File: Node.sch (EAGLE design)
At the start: 63 parts, among them J1 DF12A3.0-14DS, Q1 16MHz, U1 ATMEGA32U4QFN, U2 NRF24L01NOPAD, U3 LTC3553, U4 L3GD20, U6 LSM303DLHC, U7 BD2425NNRF0404, U9 RCLAMP0502A, X1 USBSMD

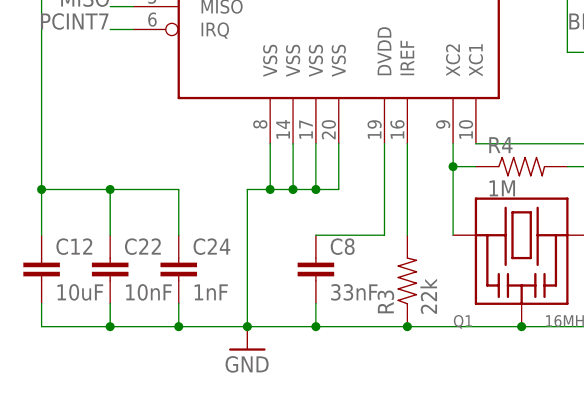
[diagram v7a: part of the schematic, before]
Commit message: start of base station
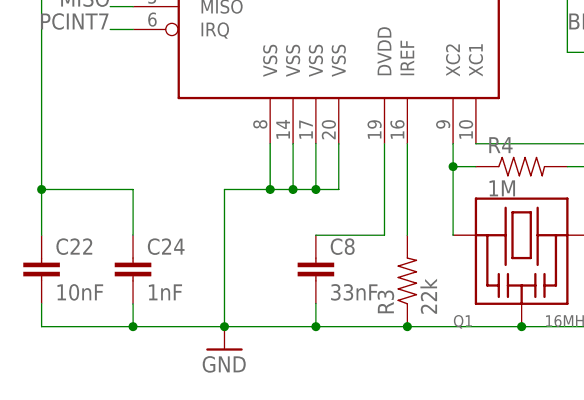
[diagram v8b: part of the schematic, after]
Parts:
- removed C12: 10uF, SparkFun:CAP0603-CAP
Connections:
- net +3V3: no longer C12.1
- net GND: no longer C12.2
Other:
- moved on the sheet: C22, C24
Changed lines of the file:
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@@
 <part name="GND9" library="supply1" deviceset="GND" device=""/>
 <part name="+3V8" library="supply1" deviceset="+3V3" device=""/>
-<part name="C12" library="SparkFun" deviceset="CAP" device="0603-CAP" value="10uF"/>
 <part name="C22" library="SparkFun" deviceset="CAP" device="0402-CAP" value="10nF"/>
 <part name="C24" library="SparkFun" deviceset="CAP" device="0402-CAP" value="1nF"/>
@@
 <instance part="U2" gate="G$1" x="43.18" y="48.26"/>
 <instance part="+3V4" gate="G$1" x="40.64" y="76.2"/>
-<instance part="GND4" gate="1" x="33.02" y="7.62"/>
+<instance part="GND4" gate="1" x="30.48" y="7.62"/>
 <instance part="C8" gate="G$1" x="40.64" y="15.24"/>
 <instance part="R3" gate="G$1" x="50.8" y="15.24" rot="R90"/>
@@
 <instance part="GND9" gate="1" x="185.42" y="121.92"/>
 <instance part="+3V8" gate="G$1" x="185.42" y="149.86"/>
-<instance part="C12" gate="G$1" x="10.16" y="15.24"/>
-<instance part="C22" gate="G$1" x="17.78" y="15.24"/>
-<instance part="C24" gate="G$1" x="25.4" y="15.24"/>
+<instance part="C22" gate="G$1" x="10.16" y="15.24"/>
+<instance part="C24" gate="G$1" x="20.32" y="15.24"/>
 <instance part="C25" gate="G$1" x="81.28" y="15.24"/>
 <instance part="C26" gate="G$1" x="91.44" y="15.24"/>
@@
 <pinref part="GND4" gate="1" pin="GND"/>
 <pinref part="U2" gate="G$1" pin="VSS@8"/>
-<wire x1="33.02" y1="25.4" x2="33.02" y2="10.16" width="0.1524" layer="91"/>
-<wire x1="33.02" y1="25.4" x2="35.56" y2="25.4" width="0.1524" layer="91"/>
+<wire x1="30.48" y1="25.4" x2="30.48" y2="10.16" width="0.1524" layer="91"/>
+<wire x1="30.48" y1="25.4" x2="35.56" y2="25.4" width="0.1524" layer="91"/>
 <wire x1="35.56" y1="25.4" x2="35.56" y2="30.48" width="0.1524" layer="91"/>
 <pinref part="U2" gate="G$1" pin="VSS@14"/>
@@
 <junction x="40.64" y="25.4"/>
 <pinref part="C8" gate="G$1" pin="2"/>
-<wire x1="33.02" y1="10.16" x2="40.64" y2="10.16" width="0.1524" layer="91"/>
+<wire x1="30.48" y1="10.16" x2="40.64" y2="10.16" width="0.1524" layer="91"/>
 <wire x1="40.64" y1="10.16" x2="40.64" y2="12.7" width="0.1524" layer="91"/>
-<junction x="33.02" y="10.16"/>
+<junction x="30.48" y="10.16"/>
 <pinref part="R3" gate="G$1" pin="1"/>
 <wire x1="50.8" y1="10.16" x2="40.64" y2="10.16" width="0.1524" layer="91"/>
@@
 <wire x1="63.5" y1="10.16" x2="50.8" y2="10.16" width="0.1524" layer="91"/>
 <junction x="50.8" y="10.16"/>
-<pinref part="C12" gate="G$1" pin="2"/>
+<pinref part="C22" gate="G$1" pin="2"/>
+<wire x1="10.16" y1="10.16" x2="20.32" y2="10.16" width="0.1524" layer="91"/>
+<wire x1="20.32" y1="10.16" x2="30.48" y2="10.16" width="0.1524" layer="91"/>
 <wire x1="10.16" y1="12.7" x2="10.16" y2="10.16" width="0.1524" layer="91"/>
-<wire x1="10.16" y1="10.16" x2="17.78" y2="10.16" width="0.1524" layer="91"/>
-<pinref part="C22" gate="G$1" pin="2"/>
-<wire x1="17.78" y1="10.16" x2="25.4" y2="10.16" width="0.1524" layer="91"/>
-<wire x1="25.4" y1="10.16" x2="33.02" y2="10.16" width="0.1524" layer="91"/>
-<wire x1="17.78" y1="12.7" x2="17.78" y2="10.16" width="0.1524" layer="91"/>
-<junction x="17.78" y="10.16"/>
 <pinref part="C24" gate="G$1" pin="2"/>
-<wire x1="25.4" y1="12.7" x2="25.4" y2="10.16" width="0.1524" layer="91"/>
-<junction x="25.4" y="10.16"/>
+<wire x1="20.32" y1="12.7" x2="20.32" y2="10.16" width="0.1524" layer="91"/>
+<junction x="20.32" y="10.16"/>
 <junction x="63.5" y="10.16"/>
 <pinref part="C25" gate="G$1" pin="2"/>
@@
 <wire x1="40.64" y1="66.04" x2="10.16" y2="66.04" width="0.1524" layer="91"/>
 <wire x1="10.16" y1="66.04" x2="10.16" y2="25.4" width="0.1524" layer="91"/>
-<wire x1="10.16" y1="25.4" x2="17.78" y2="25.4" width="0.1524" layer="91"/>
 <pinref part="C24" gate="G$1" pin="1"/>
-<wire x1="17.78" y1="25.4" x2="25.4" y2="25.4" width="0.1524" layer="91"/>
-<wire x1="25.4" y1="25.4" x2="25.4" y2="20.32" width="0.1524" layer="91"/>
-<pinref part="C12" gate="G$1" pin="1"/>
+<wire x1="10.16" y1="25.4" x2="20.32" y2="25.4" width="0.1524" layer="91"/>
+<wire x1="20.32" y1="25.4" x2="20.32" y2="20.32" width="0.1524" layer="91"/>
+<pinref part="C22" gate="G$1" pin="1"/>
 <wire x1="10.16" y1="25.4" x2="10.16" y2="20.32" width="0.1524" layer="91"/>
 <junction x="10.16" y="25.4"/>
-<pinref part="C22" gate="G$1" pin="1"/>
-<wire x1="17.78" y1="25.4" x2="17.78" y2="20.32" width="0.1524" layer="91"/>
-<junction x="17.78" y="25.4"/>
-</segment>
-<segment>
+</segment>
+<segment>
